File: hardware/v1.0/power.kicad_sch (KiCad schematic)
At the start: 38 parts, among them U1 ECP5U_12_CABGA256, U2 TLV62569DBV, U3 TLV62569DBV, U4 TLV62569DBV, Y1 SITxxxxxx-1x-33E-50.000000

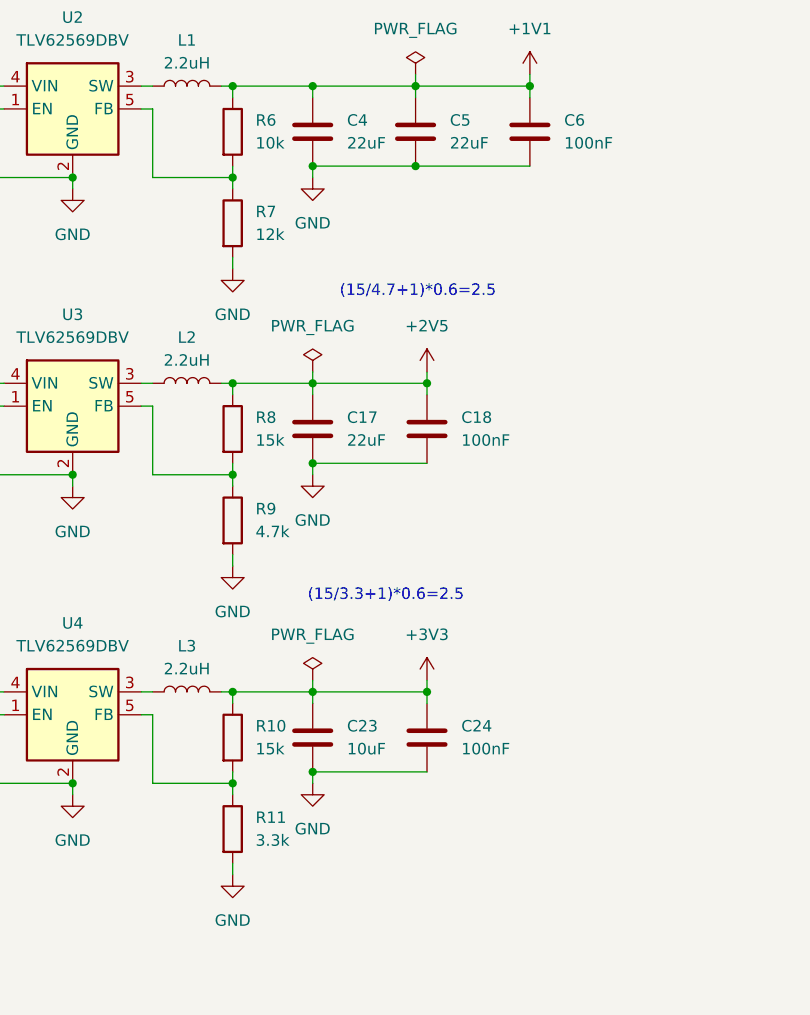
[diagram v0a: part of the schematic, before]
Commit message: Fix wrong comment text
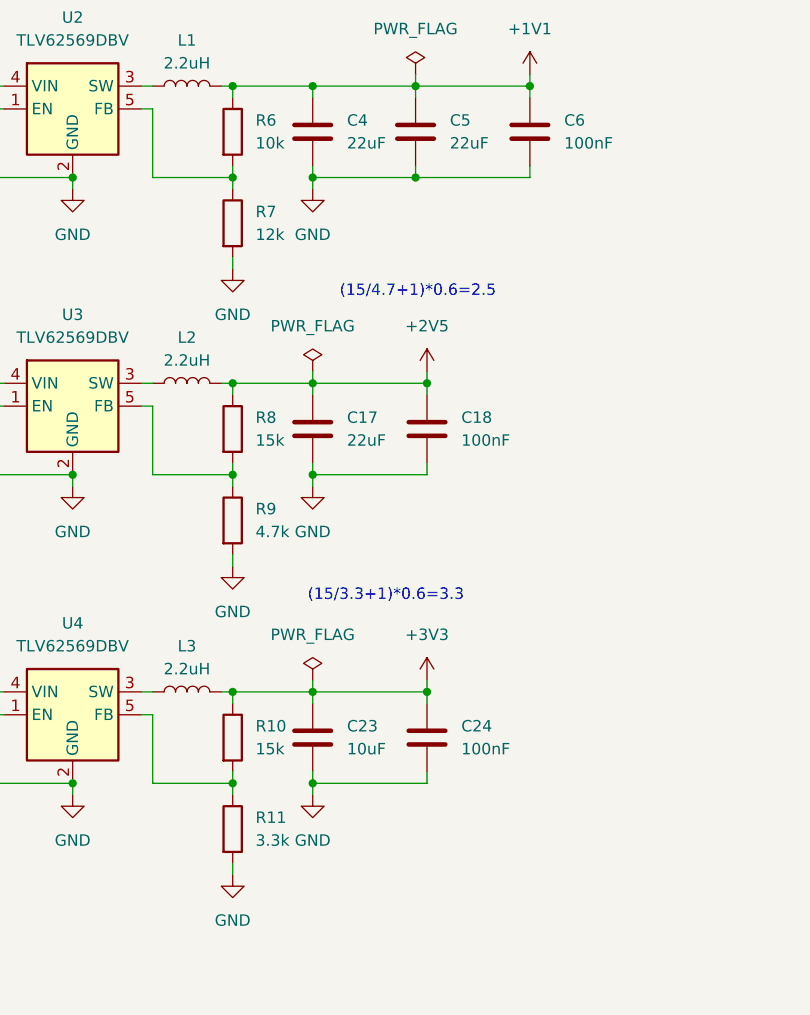
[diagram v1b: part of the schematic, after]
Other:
- note added: "(15/3.3+1)*0.6=3.3"
- note removed: "(15/3.3+1)*0.6=2.5"
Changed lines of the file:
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@@
 		)
 	)
-	(text "(15/3.3+1)*0.6=2.5"
+	(text "(15/3.3+1)*0.6=3.3"
 		(exclude_from_sim no)
 		(at 71.628 85.852 0)
@@
 	)
 	(junction
-		(at 63.5 38.1)
+		(at 54.61 72.39)
 		(diameter 0)
 		(color 0 0 0 0)
 	)
 	(junction
-		(at 54.61 72.39)
+		(at 63.5 106.68)
 		(diameter 0)
 		(color 0 0 0 0)
@@
 	)
 	(junction
-		(at 35.56 151.13)
+		(at 63.5 39.37)
 		(diameter 0)
 		(color 0 0 0 0)
 	)
 	(junction
-		(at 63.5 29.21)
+		(at 35.56 151.13)
 		(diameter 0)
 		(color 0 0 0 0)
 	)
 	(junction
-		(at 74.93 38.1)
+		(at 63.5 29.21)
 		(diameter 0)
 		(color 0 0 0 0)
@@
 	)
 	(junction
+		(at 63.5 72.39)
+		(diameter 0)
+		(color 0 0 0 0)
+	)
+	(junction
 		(at 24.13 29.21)
 		(diameter 0)
@@
 	)
 	(junction
-		(at 201.93 59.69)
+		(at 74.93 39.37)
 		(diameter 0)
 		(color 0 0 0 0)
 	)
 	(junction
-		(at 187.96 71.12)
+		(at 201.93 59.69)
 		(diameter 0)
 		(color 0 0 0 0)
 	)
 	(junction
-		(at 63.5 71.12)
+		(at 187.96 71.12)
 		(diameter 0)
 		(color 0 0 0 0)
@@
 	)
 	(junction
-		(at 63.5 105.41)
-		(diameter 0)
-		(color 0 0 0 0)
-	)
-	(junction
 		(at 24.13 96.52)
 		(diameter 0)
@@
 	(wire
 		(pts
-			(xy 63.5 106.68) (xy 63.5 105.41)
+			(xy 63.5 107.95) (xy 63.5 106.68)
 		)
 		(stroke
@@
 	(wire
 		(pts
-			(xy 63.5 39.37) (xy 63.5 38.1)
+			(xy 63.5 40.64) (xy 63.5 39.37)
 		)
 		(stroke
@@
 	(wire
 		(pts
-			(xy 74.93 38.1) (xy 87.63 38.1)
+			(xy 74.93 39.37) (xy 87.63 39.37)
 		)
 		(stroke
@@
 	(wire
 		(pts
-			(xy 63.5 71.12) (xy 76.2 71.12)
+			(xy 63.5 72.39) (xy 76.2 72.39)
 		)
 		(stroke
@@
 	(wire
 		(pts
+			(xy 63.5 72.39) (xy 63.5 71.12)
+		)
+		(stroke
+			(width 0)
+			(type default)
+		)
+	)
+	(wire
+		(pts
 			(xy 63.5 95.25) (xy 63.5 96.52)
 		)
@@
 	(wire
 		(pts
+			(xy 63.5 106.68) (xy 63.5 105.41)
+		)
+		(stroke
+			(width 0)
+			(type default)
+		)
+	)
+	(wire
+		(pts
 			(xy 27.94 156.21) (xy 27.94 151.13)
 		)
@@
 	(wire
 		(pts
+			(xy 76.2 72.39) (xy 76.2 71.12)
+		)
+		(stroke
+			(width 0)
+			(type default)
+		)
+	)
+	(wire
+		(pts
 			(xy 187.96 71.12) (xy 187.96 72.39)
 		)
@@
 	(wire
 		(pts
+			(xy 87.63 39.37) (xy 87.63 38.1)
+		)
+		(stroke
+			(width 0)
+			(type default)
+		)
+	)
+	(wire
+		(pts
 			(xy 27.94 64.77) (xy 29.21 64.77)
 		)
@@
 	(wire
 		(pts
+			(xy 63.5 39.37) (xy 63.5 38.1)
+		)
+		(stroke
+			(width 0)
+			(type default)
+		)
+	)
+	(wire
+		(pts
 			(xy 198.12 71.12) (xy 209.55 71.12)
 		)
@@
 	(wire
 		(pts
-			(xy 63.5 72.39) (xy 63.5 71.12)
+			(xy 63.5 73.66) (xy 63.5 72.39)
 		)
 		(stroke
@@
 	(wire
 		(pts
-			(xy 74.93 38.1) (xy 63.5 38.1)
+			(xy 74.93 39.37) (xy 63.5 39.37)
 		)
 		(stroke
@@
 	(wire
 		(pts
+			(xy 74.93 39.37) (xy 74.93 38.1)
+		)
+		(stroke
+			(width 0)
+			(type default)
+		)
+	)
+	(wire
+		(pts
 			(xy 76.2 62.23) (xy 76.2 63.5)
 		)
@@
 	(wire
 		(pts
-			(xy 63.5 105.41) (xy 76.2 105.41)
+			(xy 63.5 106.68) (xy 76.2 106.68)
 		)
 		(stroke
@@
 	(wire
 		(pts
+			(xy 76.2 106.68) (xy 76.2 105.41)
+		)
+		(stroke
+			(width 0)
+			(type default)
+		)
+	)
+	(wire
+		(pts
 			(xy 45.72 64.77) (xy 44.45 64.77)
 		)
@@
 	(symbol
 		(lib_id "power:GND")
-		(at 63.5 106.68 0)
+		(at 63.5 107.95 0)
 		(unit 1)
 		(exclude_from_sim no)
@@
 		(fields_autoplaced yes)
 		(property "Reference" "#PWR040"
-			(at 63.5 113.03 0)
+			(at 63.5 114.3 0)
 			(effects
 				(font
@@
 		)
 		(property "Value" "GND"
-			(at 63.5 111.76 0)
+			(at 63.5 113.03 0)
 			(effects
 				(font
@@
 		)
 		(property "Footprint" ""
-			(at 63.5 106.68 0)
+			(at 63.5 107.95 0)
 			(effects
 				(font
@@
 		)
 		(property "Datasheet" ""
-			(at 63.5 106.68 0)
+			(at 63.5 107.95 0)
 			(effects
 				(font
@@
 		)
 		(property "Description" "Power symbol creates a global label with name \"GND\" , ground"
-			(at 63.5 106.68 0)
+			(at 63.5 107.95 0)
 			(effects
 				(font
@@
 	(symbol
 		(lib_id "power:GND")
-		(at 63.5 39.37 0)
+		(at 63.5 40.64 0)
 		(unit 1)
 		(exclude_from_sim no)
@@
 		(fields_autoplaced yes)
 		(property "Reference" "#PWR025"
-			(at 63.5 45.72 0)
+			(at 63.5 46.99 0)
 			(effects
 				(font
@@
 		)
 		(property "Value" "GND"
-			(at 63.5 44.45 0)
+			(at 63.5 45.72 0)
 			(effects
 				(font
@@
 		)
 		(property "Footprint" ""
-			(at 63.5 39.37 0)
+			(at 63.5 40.64 0)
 			(effects
 				(font
@@
 		)
 		(property "Datasheet" ""
-			(at 63.5 39.37 0)
+			(at 63.5 40.64 0)
 			(effects
 				(font
@@
 		)
 		(property "Description" "Power symbol creates a global label with name \"GND\" , ground"
-			(at 63.5 39.37 0)
+			(at 63.5 40.64 0)
 			(effects
 				(font
@@
 	(symbol
 		(lib_id "power:GND")
-		(at 63.5 72.39 0)
+		(at 63.5 73.66 0)
 		(unit 1)
 		(exclude_from_sim no)
@@
 		(fields_autoplaced yes)
 		(property "Reference" "#PWR033"
-			(at 63.5 78.74 0)
+			(at 63.5 80.01 0)
 			(effects
 				(font
@@
 		)
 		(property "Value" "GND"
-			(at 63.5 77.47 0)
+			(at 63.5 78.74 0)
 			(effects
 				(font
@@
 		)
 		(property "Footprint" ""
-			(at 63.5 72.39 0)
+			(at 63.5 73.66 0)
 			(effects
 				(font
@@
 		)
 		(property "Datasheet" ""
-			(at 63.5 72.39 0)
+			(at 63.5 73.66 0)
 			(effects
 				(font
@@
 		)
 		(property "Description" "Power symbol creates a global label with name \"GND\" , ground"
-			(at 63.5 72.39 0)
+			(at 63.5 73.66 0)
 			(effects
 				(font
